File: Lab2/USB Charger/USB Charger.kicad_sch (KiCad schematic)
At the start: 0 parts

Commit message: finished USB Charger Schematic, awaiting checkoff
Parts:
- added C1: 1 uF, symbol Device:C
- added C2, C3: 22uF, symbol Device:C_Small_US
- added D1, D2: D_Schottky, symbol Device:D_Schottky
- added D3: LED, symbol Device:LED
- added F1: Polyfuse, symbol Device:Polyfuse
- added J1: USB_A, symbol Connector:USB_A
- added J2: USB_B_Micro, symbol Connector:USB_B_Micro
- added J4: Conn_01x02, symbol Connector_Generic:Conn_01x02
- added L1: 1 uH, symbol Device:L
- added P1: USB_C_Plug_USB2.0, symbol Connector:USB_C_Plug_USB2.0
- added R1, R2: 22K, symbol Device:R
- added R3: 732KΩ, symbol Device:R_Small_US
- added R4: 100KΩ, symbol Device:R_Small_US
- added R5: 150 Ω, symbol Device:R
- added U1: TPS61023DRLR, DRL0006A, symbol 2025-09-26_03-45-56:TPS61023DRLR
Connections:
- new net: R3.2, R4.1, U1.1 (FB)
- new net: C1.1, D1.1 (K), D2.1 (K), F1.1, F1.2, L1.1, U1.3 (VIN)
- new net: L1.2, U1.5 (SW)
- new net: P1.B5 (VCONN), R2.2
- new net: D1.2 (A), J2.1 (VBUS)
- new net: J2.2 (D-), J2.3 (D+)
- new net: D2.2 (A), J4.2 (Pin_2)
- new net: P1.A5 (CC), R1.2
- new net: P1.A6 (D+), P1.A7 (D-)
- new net: D3.2 (A), R5.2
- new net: J1.2 (D-), J1.3 (D+)
- new net +5V: C2.1, C3.1, J1.1 (VBUS), P1.A4 (VBUS), P1.A9 (VBUS), P1.B4 (VBUS), P1.B9 (VBUS), R1.1, R2.1, R3.1, R5.1, U1.6 (VOUT)
- new net GND: C1.2, C2.2, C3.2, D3.1 (K), J1.4 (GND), J1.5 (Shield), J2.4 (ID), J2.5 (GND), J2.6 (Shield), J4.1 (Pin_1), P1.A1 (GND), P1.A12 (GND), P1.B1 (GND), P1.B12 (GND), P1.S1 (SHIELD), R4.2, U1.4 (GND)
- no-connect marks 0 -> 1
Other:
- note added: "Boast IC (TPS61023)"
- note added: "Input"
- note added: "Power Receptacle"

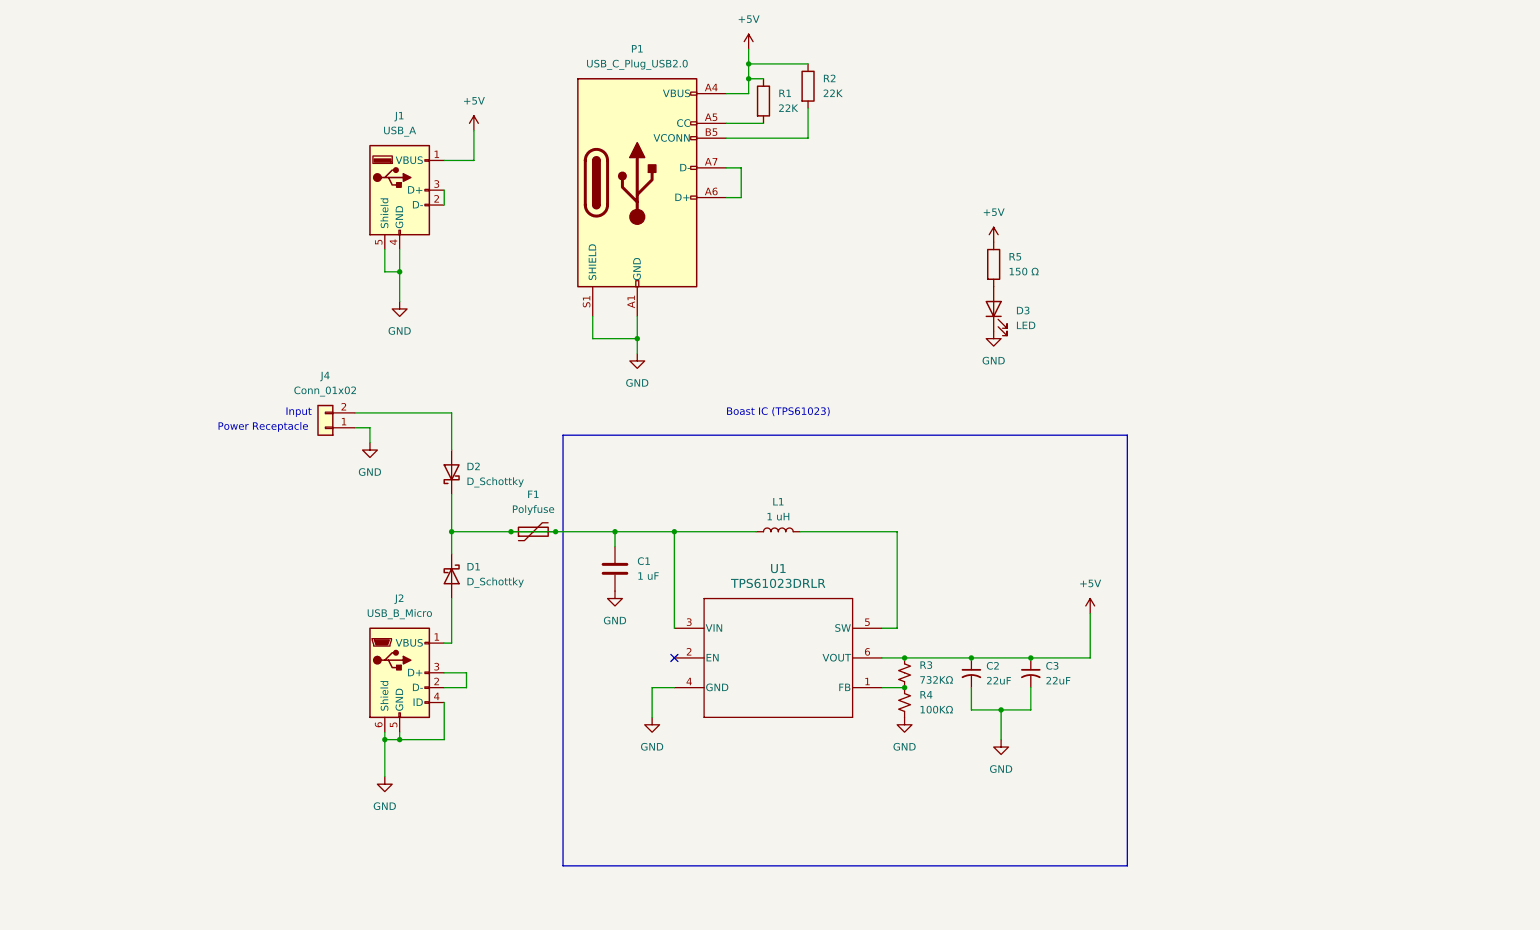
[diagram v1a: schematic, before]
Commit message: Finished USB Charger Schematic
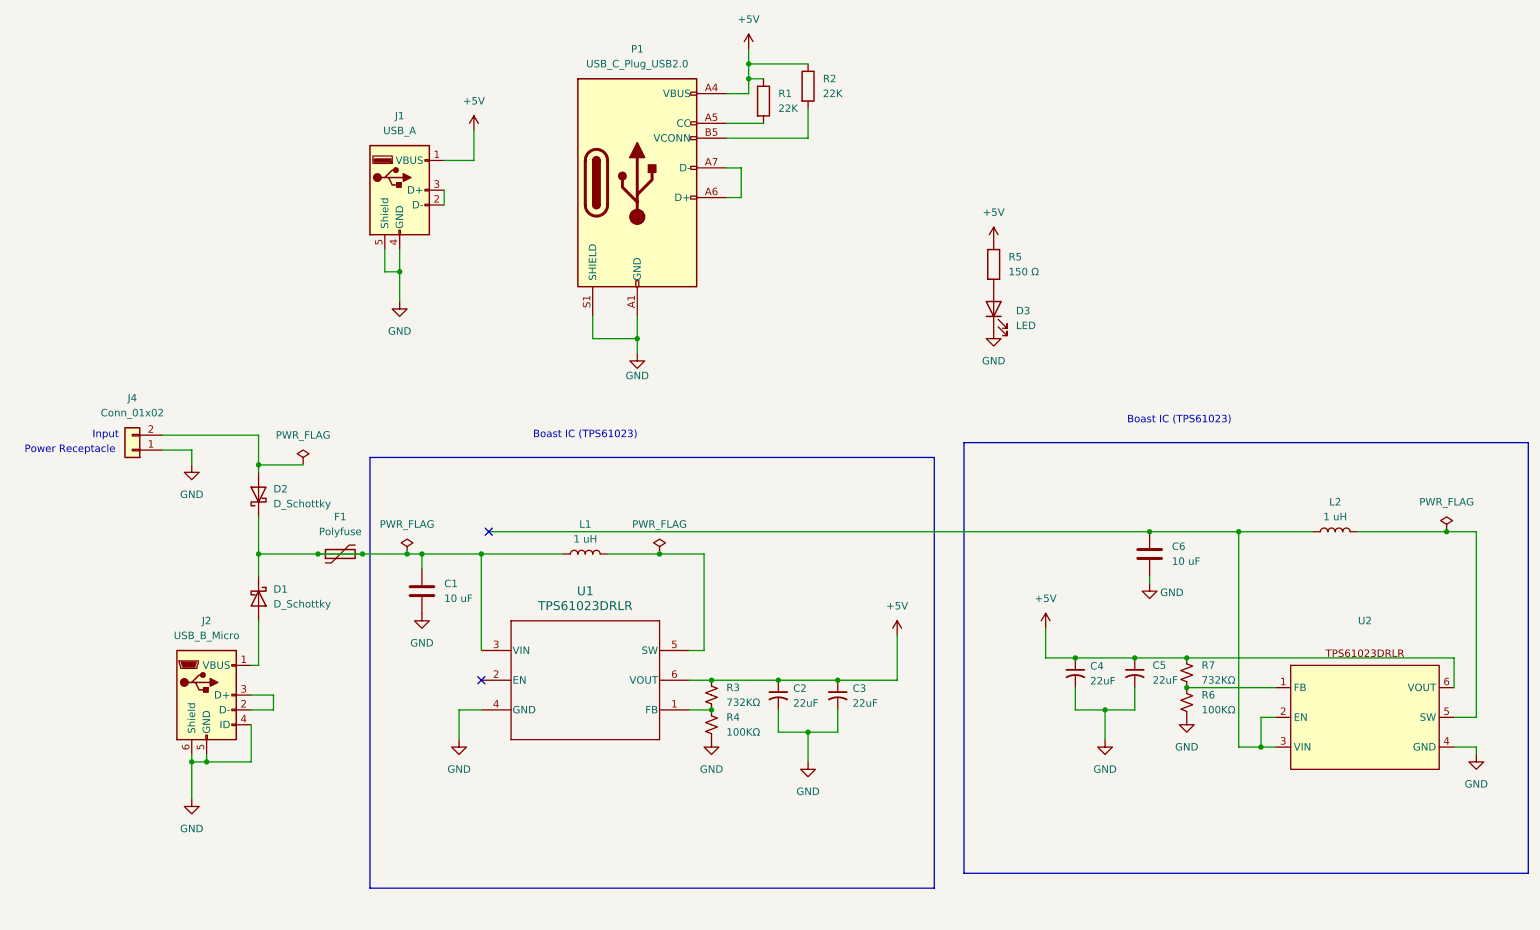
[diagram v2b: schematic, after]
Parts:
- added C4, C5: 22uF, Capacitor_SMD:C_0603_1608Metric_Pad1.08x0.95mm_HandSolder, symbol Device:C_Small_US
- added C6: 10 uF, Capacitor_SMD:C_0402_1005Metric, symbol Device:C
- added L2: 1 uH, symbol Device:L
- added R6: 100KΩ, symbol Device:R_Small_US
- added R7: 732KΩ, symbol Device:R_Small_US
- added U2: ~, symbol Hope Symbol Library:TPS61023DRLR_Siwen
- C1: value 1 uF -> 10 uF; footprint (none) -> Capacitor_SMD:C_0402_1005Metric
- C2, C3: footprint (none) -> Capacitor_SMD:C_0603_1608Metric_Pad1.08x0.95mm_HandSolder
- D1, D2: footprint (none) -> Diode_SMD:D_SMA-SMB_Universal_Handsoldering
- D3: footprint (none) -> LED_SMD:LED_0805_2012Metric_Pad1.15x1.40mm_HandSolder
- F1: footprint (none) -> Fuse:Fuse_1812_4532Metric_Pad1.30x3.40mm_HandSolder
- J1: footprint (none) -> Connector_USB:USB_A_Receptacle_GCT_USB1046
- J2, J4: footprint (none) -> 10118192_0002LF:AMPHENOL_10118192-0002LF
- U1: symbol 2025-09-26_03-45-56:TPS61023DRLR -> Ultra Librarian TPS61023DRLR:TPS61023DRLR
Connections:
- net +5V: now also C4.1, C5.1, R7.1, U2.6 (VOUT)
- net GND: now also C4.2, C5.2, C6.2, R6.2, U2.4 (GND)
- new net: C6.1, L2.1, U2.2 (EN), U2.3 (VIN)
- new net: L2.2, U2.5 (SW)
- new net: R6.1, R7.2, U2.1 (FB)
- no-connect marks 1 -> 2
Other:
- moved on the sheet: C1, C2, C3, D1, D2, F1, J2, J4, L1, R3, R4, U1

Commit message: Finished USB Charger Layout, awaiting checkoff
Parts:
- removed C1: 10 uF, Capacitor_SMD:C_0402_1005Metric, symbol Device:C
- removed C2, C3: 22uF, Capacitor_SMD:C_0603_1608Metric_Pad1.08x0.95mm_HandSolder, symbol Device:C_Small_US
- removed L1: 1 uH, symbol Device:L
- removed R3: 732KΩ, symbol Device:R_Small_US
- removed R4: 100KΩ, symbol Device:R_Small_US
- removed U1: TPS61023DRLR, DRL0006A, symbol Ultra Librarian TPS61023DRLR:TPS61023DRLR
- J2: symbol Connector:USB_B_Micro -> 10118192-0002LF:10118192-0002LF; MANUFACTURER (none) -> Amphenol; MAXIMUM_PACKAGE_HEIGHT (none) -> 2.8mm; PARTREV (none) -> B; STANDARD (none) -> Manufacturer Recommendations
- J4: footprint 10118192_0002LF:AMPHENOL_10118192-0002LF -> Connector_PinHeader_2.54mm:PinHeader_1x02_P2.54mm_Vertical
- L2: footprint (none) -> custom:SRP6540-1R0M
- P1: footprint (none) -> Connector_USB:USB_C_Receptacle_GCT_USB4105-xx-A_16P_TopMnt_Horizontal
- R1, R2: footprint (none) -> Resistor_SMD:R_0603_1608Metric
- R5: footprint (none) -> Resistor_SMD:R_0805_2012Metric
- R6, R7: footprint (none) -> Resistor_SMD:R_0402_1005Metric
- U2: footprint (none) -> Package_TO_SOT_SMD:SOT-666
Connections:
- net GND: now also J2.S1 (SHIELD), J2.S2 (SHIELD__1), J2.S3 (SHIELD__2), J2.S4 (SHIELD__3), J2.S5 (SHIELD__4), J2.S6 (SHIELD__5); no longer J2.6 (Shield)
- net at D1.1 (K), D2.1 (K), F1.1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: now also C6.1, L2.1, U2.2 (EN), U2.3 (VIN)
- no-connect marks 2 -> 0
